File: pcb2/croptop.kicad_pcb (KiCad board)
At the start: 4 copper layers, 190.1 x 107.2 mm, 341 parts, among them J1 TSM-106-01-L-SV, J10 1702474, J11 1702474, J12 1702474, J13 1702474, J14 1702474, J15 TSM-112-01-L-DV, J16 DM3D-SF, J2 0473460001, J3 87583-2010BLF, J4 TSM-102-01-L-DV, J5 686104183422, J6 62684-402100ALF, J7 1702474, J8 1702474, J9 1702474, Q1 BSS138, Q2 BSS84, Q3 Q2319ADS-T1-GE3, Q4 BSS138, Q5 BSS138, Q6 BSS138, SW1 SW_Push, SW2 SW_Push, SW3 SW_Push, SW4 SW_Push, U1 PIC32MX795F512L, U10 TPD4E1U06DBV, U11 TPD4E1U06DBV, U12 TPD4E1U06DBV, U13 TPD4E1U06DBV, U14 TPD4E1U06DBV, U15 TPD4E1U06DBV, U16 TPD4E1U06DBV, U17 TPD4E1U06DBV, U18 74HCT125D653, U19 AP22802AW5, U2 REG71055DDC, U20 AD7799, U21 AP22802AW5, U22 TPD4E1U06DBV, U23 AP22802AW5, U24 TPD4E1U06DBV, U25 TPD4E1U06DBV, U26 TPD4E1U06DBV, U27 DRV8872, U28 DRV8825, U29 AP22802AW5, U3 AP22802AW5, U30 TPD4E1U06DBV, U31 TPD4E1U06DBV, U32 AP22802AW5, U33 AP22802AW5, U34 TPD4E1U06DBV, U35 TPD4E1U06DBV, U36 AP22802AW5, U37 TPD4E1U06DBV, U38 TPD4E1U06DBV, U39 LIS3DSHTR, U4 TPS61169DCK, U40 CAM-M8C-0, U41 Si7006-A20, U5 TPS62131RGT, U6 TPS70950DBV, U7 TPD4E1U06DBV, U8 TPD4E1U06DBV, U9 FT812Q, Y1 ABLS-8.000MHZ-B4-T, Y2 ABLS-12.000MHZ-B2-T, Y3 ABS07-32.768KHZ-1-T

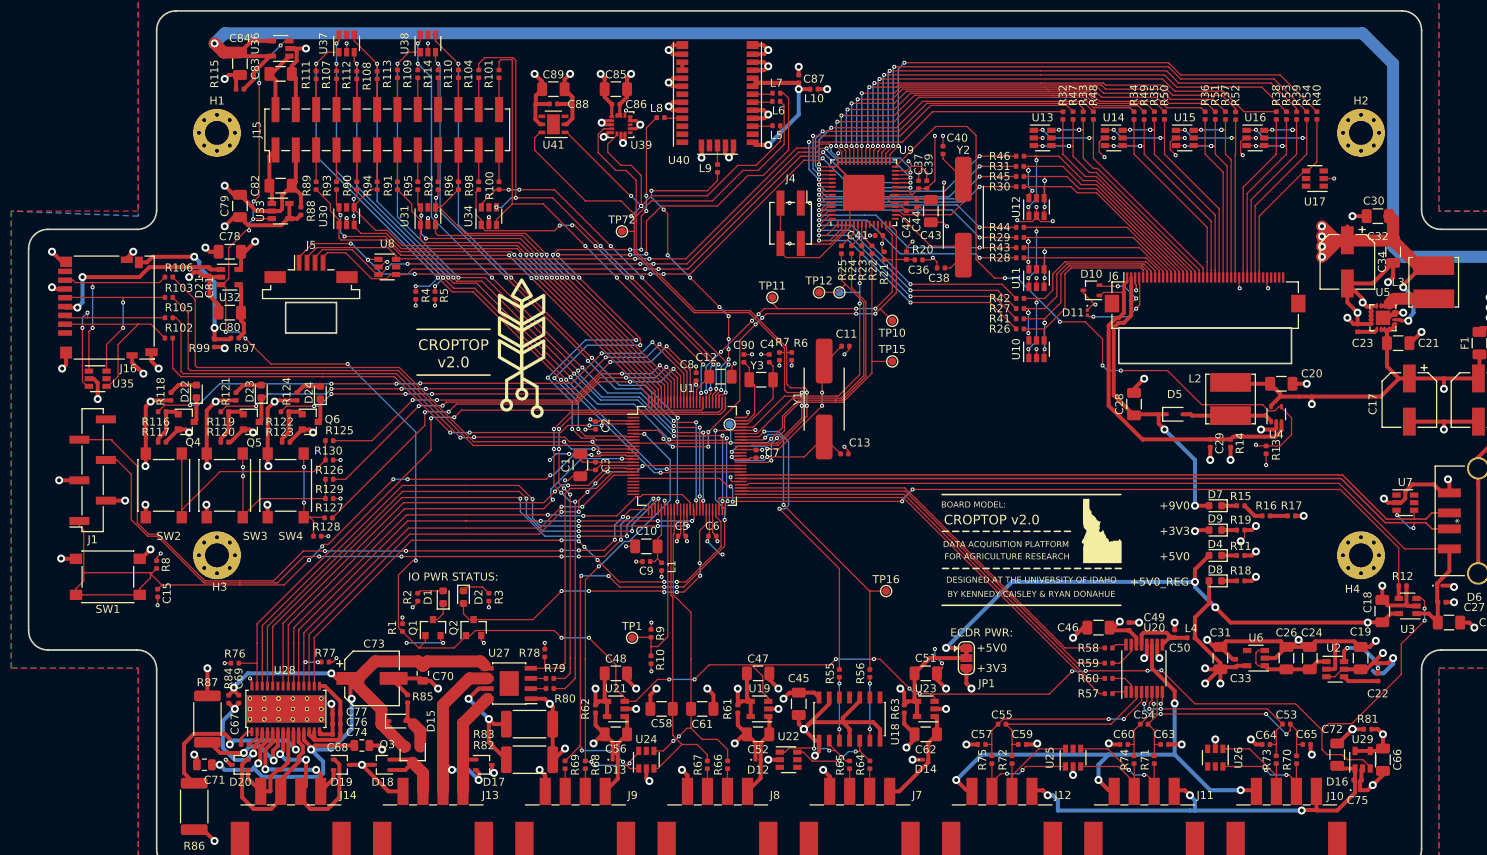
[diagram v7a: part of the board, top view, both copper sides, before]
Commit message: Fixed Screen alignment
- Fixed pin alignment of LCD screen
- Pins now properly align with the ribbon cables of the LCD screen
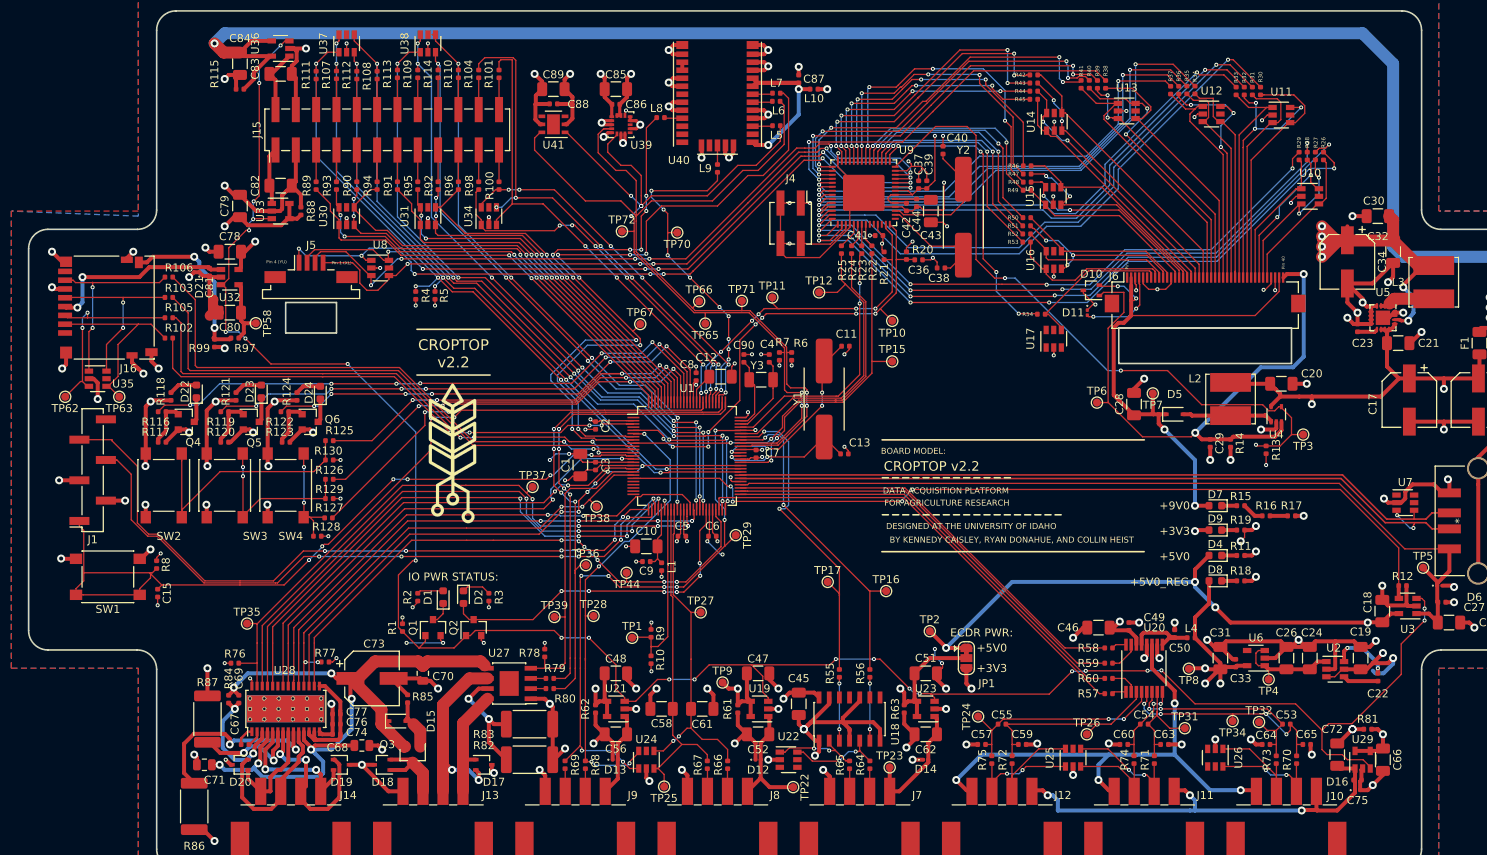
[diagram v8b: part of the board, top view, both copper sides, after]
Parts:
- removed the G*** at (186.4, 120.0)
- removed H1, H2, H3, H4: 3mm, MountingHole:MountingHole_3mm_Pad_Via
- removed TP13, TP14: TestPoint, TestPoint:TestPoint_Pad_D1.0mm
- added TP17: TestPoint, TestPoint:TestPoint_Pad_D1.0mm, F.Cu at (152.2, 126.4)
- added TP2: TestPoint, TestPoint:TestPoint_Pad_D1.0mm, F.Cu at (165.0, 132.5)
- added TP22: TestPoint, TestPoint:TestPoint_Pad_D1.0mm, F.Cu at (147.9, 152.0)
- added TP23: TestPoint, TestPoint:TestPoint_Pad_D1.0mm, F.Cu at (160.0, 149.5)
- added TP24: TestPoint, TestPoint:TestPoint_Pad_D1.0mm, F.Cu at (171.0, 143.2)
- added TP25: TestPoint, TestPoint:TestPoint_Pad_D1.0mm, F.Cu at (131.8, 152.0)
- added TP26: TestPoint, TestPoint:TestPoint_Pad_D1.0mm, F.Cu at (184.6, 145.4)
- added TP27: TestPoint, TestPoint:TestPoint_Pad_D1.0mm, F.Cu at (136.3, 130.2)
- added TP28: TestPoint, TestPoint:TestPoint_Pad_D1.0mm, F.Cu at (122.9, 130.6)
- added TP29: TestPoint, TestPoint:TestPoint_Pad_D1.0mm, F.Cu at (140.7, 120.5)
- added TP3: TestPoint, TestPoint:TestPoint_Pad_D1.0mm, F.Cu at (211.6, 108.0)
- added TP31: TestPoint, TestPoint:TestPoint_Pad_D1.0mm, F.Cu at (196.8, 144.7)
- added TP32: TestPoint, TestPoint:TestPoint_Pad_D1.0mm, F.Cu at (206.1, 143.9)
- added TP34: TestPoint, TestPoint:TestPoint_Pad_D1.0mm, F.Cu at (202.8, 143.8)
- added TP35: TestPoint, TestPoint:TestPoint_Pad_D1.0mm, F.Cu at (79.6, 131.6)
- added TP36: TestPoint, TestPoint:TestPoint_Pad_D1.0mm, F.Cu at (122.0, 124.3)
- added TP37: TestPoint, TestPoint:TestPoint_Pad_D1.0mm, F.Cu at (115.3, 114.5)
- added TP38: TestPoint, TestPoint:TestPoint_Pad_D1.0mm, F.Cu at (123.3, 117.0)
- added TP39: TestPoint, TestPoint:TestPoint_Pad_D1.0mm, F.Cu at (118.0, 130.7)
- added TP4: TestPoint, TestPoint:TestPoint_Pad_D1.0mm, F.Cu at (207.3, 138.6)
- added TP44: TestPoint, TestPoint:TestPoint_Pad_D1.0mm, F.Cu at (127.1, 125.2)
- added TP5: TestPoint, TestPoint:TestPoint_Pad_D1.0mm, F.Cu at (226.6, 124.6)
- added TP58: TestPoint, TestPoint:TestPoint_Pad_D1.0mm, F.Cu at (80.7, 94.0)
- added TP6: TestPoint, TestPoint:TestPoint_Pad_D1.0mm, F.Cu at (185.9, 103.9)
- added TP62: TestPoint, TestPoint:TestPoint_Pad_D1.0mm, F.Cu at (56.9, 103.2)
- added TP63: TestPoint, TestPoint:TestPoint_Pad_D1.0mm, F.Cu at (63.7, 103.2)
- added TP65: TestPoint, TestPoint:TestPoint_Pad_D1.0mm, F.Cu at (136.9, 94.1)
- added TP66: TestPoint, TestPoint:TestPoint_Pad_D1.0mm, F.Cu at (136.1, 91.3)
- added TP67: TestPoint, TestPoint:TestPoint_Pad_D1.0mm, F.Cu at (128.8, 94.1)
- added TP7: TestPoint, TestPoint:TestPoint_Pad_D1.0mm, F.Cu at (192.8, 102.8)
- added TP70: TestPoint, TestPoint:TestPoint_Pad_D1.0mm, F.Cu at (133.4, 82.7)
- added TP71: TestPoint, TestPoint:TestPoint_Pad_D1.0mm, F.Cu at (141.5, 91.2)
- added TP8: TestPoint, TestPoint:TestPoint_Pad_D1.0mm, F.Cu at (197.4, 137.2)
- added TP9: TestPoint, TestPoint:TestPoint_Pad_D1.0mm, F.Cu at (139.1, 138.9)
- moved R26 43.7 mm to (214.2, 73.1), turned to 90 degrees
- moved R27 41.6 mm to (213.2, 73.1), turned to 90 degrees
- moved R54 41.4 mm to (178.9, 92.9), turned to 180 degrees
- moved U10 39.2 mm to (212.5, 78.2), turned to 0 degrees
- moved U17 38.3 mm to (180.5, 96.0), turned to 90 degrees
- moved R28 38.1 mm to (212.2, 73.1), turned to 90 degrees
- moved U11 36.8 mm to (208.9, 68.0), turned to 0 degrees
- moved R29 36.3 mm to (211.1, 73.1), turned to 90 degrees
- moved R53 36.1 mm to (177.1, 83.9), turned to 180 degrees
- moved R30 32.4 mm to (206.3, 65.0), turned to 90 degrees
- moved R31 30.6 mm to (205.3, 65.0), turned to 90 degrees
- moved R41 30.3 mm to (183.9, 64.2), turned to 90 degrees
- moved R52 30.0 mm to (177.1, 82.9), turned to 180 degrees
- moved U16 29.4 mm to (180.5, 86.1), turned to 90 degrees
- moved R40 28.7 mm to (184.9, 64.2)
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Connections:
- J5 pad 1: GPU_X+ -> GPU_Y+
- J5 pad 2: GPU_Y- -> GPU_X+
- J5 pad 3: GPU_X- -> GPU_Y-
- J5 pad 4: GPU_Y+ -> GPU_X-
- J6 pad 1: LCD_K -> Net-(J6-Pad1)
- J6 pad 12: Net-(J6-Pad12) -> DGND
- J6 pad 2: LCD_A -> Net-(J6-Pad2)
- J6 pad 29: DGND -> Net-(J6-Pad29)
- J6 pad 3: DGND -> Net-(J6-Pad3)
- J6 pad 36: DGND -> Net-(J6-Pad36)
- J6 pad 37: Net-(J6-Pad37) -> +3V3
- J6 pad 38: Net-(J6-Pad38) -> DGND
- J6 pad 39: Net-(J6-Pad39) -> LCD_A
- J6 pad 4: +3V3 -> Net-(J6-Pad4)
- J6 pad 40: Net-(J6-Pad40) -> LCD_K
- J6 pad 5: Net-(J6-Pad5) -> DGND
- R26 pad 1: Net-(J6-Pad5) -> Net-(J6-Pad36)
- R27 pad 1: Net-(J6-Pad7) -> Net-(J6-Pad35)
- R28 pad 1: Net-(J6-Pad9) -> Net-(J6-Pad34)
- R29 pad 1: Net-(J6-Pad11) -> Net-(J6-Pad33)
- R30 pad 1: Net-(J6-Pad13) -> Net-(J6-Pad32)
- R31 pad 1: Net-(J6-Pad15) -> Net-(J6-Pad31)
- R32 pad 1: Net-(J6-Pad17) -> Net-(J6-Pad30)
- R33 pad 1: Net-(J6-Pad19) -> Net-(J6-Pad29)
- R34 pad 1: Net-(J6-Pad21) -> Net-(J6-Pad28)
- R35 pad 1: Net-(J6-Pad23) -> Net-(J6-Pad27)
- R36 pad 1: Net-(J6-Pad25) -> Net-(J6-Pad26)
- R37 pad 1: Net-(J6-Pad27) -> Net-(J6-Pad25)
- R38 pad 1: Net-(J6-Pad30) -> Net-(J6-Pad24)
- R39 pad 1: Net-(J6-Pad32) -> Net-(J6-Pad23)
- R40 pad 1: Net-(J6-Pad34) -> Net-(J6-Pad22)
- R41 pad 1: Net-(J6-Pad6) -> Net-(J6-Pad21)
- R42 pad 1: Net-(J6-Pad8) -> Net-(J6-Pad20)
- R43 pad 1: Net-(J6-Pad10) -> Net-(J6-Pad19)
- R44 pad 1: Net-(J6-Pad12) -> Net-(J6-Pad18)
- R45 pad 1: Net-(J6-Pad14) -> Net-(J6-Pad17)
- R47 pad 1: Net-(J6-Pad18) -> Net-(J6-Pad15)
- R48 pad 1: Net-(J6-Pad20) -> Net-(J6-Pad14)
- R49 pad 1: Net-(J6-Pad22) -> Net-(J6-Pad13)
- R50 pad 1: Net-(J6-Pad24) -> Net-(J6-Pad11)
- R51 pad 1: Net-(J6-Pad26) -> Net-(J6-Pad10)
- R52 pad 1: Net-(J6-Pad28) -> Net-(J6-Pad9)
- R53 pad 1: Net-(J6-Pad31) -> Net-(J6-Pad8)
- R54 pad 1: Net-(J6-Pad33) -> Net-(J6-Pad7)
- U10 pad 1: Net-(J6-Pad8) -> Net-(J6-Pad33)
- U10 pad 3: Net-(J6-Pad6) -> Net-(J6-Pad35)
- U10 pad 4: Net-(J6-Pad5) -> Net-(J6-Pad36)
- U10 pad 6: Net-(J6-Pad7) -> Net-(J6-Pad34)
- U11 pad 1: Net-(J6-Pad12) -> Net-(J6-Pad29)
- U11 pad 3: Net-(J6-Pad10) -> Net-(J6-Pad31)
- U11 pad 4: Net-(J6-Pad9) -> Net-(J6-Pad32)
- U11 pad 6: Net-(J6-Pad11) -> Net-(J6-Pad30)
- U12 pad 1: Net-(J6-Pad16) -> Net-(J6-Pad25)
- U12 pad 3: Net-(J6-Pad14) -> Net-(J6-Pad27)
- U12 pad 4: Net-(J6-Pad13) -> Net-(J6-Pad28)
- U12 pad 6: Net-(J6-Pad15) -> Net-(J6-Pad26)
- U13 pad 1: Net-(J6-Pad20) -> Net-(J6-Pad21)
- U13 pad 3: Net-(J6-Pad18) -> Net-(J6-Pad23)
- U13 pad 4: Net-(J6-Pad17) -> Net-(J6-Pad24)
- U13 pad 6: Net-(J6-Pad19) -> Net-(J6-Pad22)
- U14 pad 1: Net-(J6-Pad24) -> Net-(J6-Pad17)
- U14 pad 3: Net-(J6-Pad22) -> Net-(J6-Pad19)
- U14 pad 4: Net-(J6-Pad21) -> Net-(J6-Pad20)
- U14 pad 6: Net-(J6-Pad23) -> Net-(J6-Pad18)
- U15 pad 1: Net-(J6-Pad28) -> Net-(J6-Pad13)
- U15 pad 3: Net-(J6-Pad26) -> Net-(J6-Pad15)
- U15 pad 4: Net-(J6-Pad25) -> Net-(J6-Pad16)
- U15 pad 6: Net-(J6-Pad27) -> Net-(J6-Pad14)
- U16 pad 1: Net-(J6-Pad33) -> Net-(J6-Pad8)
- U16 pad 3: Net-(J6-Pad31) -> Net-(J6-Pad10)
- U16 pad 4: Net-(J6-Pad30) -> Net-(J6-Pad11)
- U16 pad 6: Net-(J6-Pad32) -> Net-(J6-Pad9)
- U17 pad 4: Net-(J6-Pad34) -> Net-(J6-Pad7)
- U8 pad 1: GPU_X+ -> GPU_Y+
- U8 pad 3: GPU_X- -> GPU_Y-
- U8 pad 4: GPU_Y+ -> GPU_X-
- U8 pad 6: GPU_Y- -> GPU_X+
- U9 pad 1: Net-(R41-Pad2) -> Net-(R27-Pad2)
- U9 pad 29: Net-(R40-Pad2) -> Net-(R54-Pad2)
- U9 pad 30: Net-(R54-Pad2) -> Net-(R53-Pad2)
- U9 pad 31: Net-(R39-Pad2) -> Net-(R52-Pad2)
- U9 pad 32: Net-(R53-Pad2) -> Net-(R51-Pad2)
- U9 pad 33: Net-(R38-Pad2) -> Net-(R50-Pad2)
- U9 pad 34: Net-(R52-Pad2) -> Net-(R49-Pad2)
- U9 pad 35: Net-(R37-Pad2) -> Net-(R48-Pad2)
- U9 pad 36: Net-(R51-Pad2) -> Net-(R47-Pad2)
- U9 pad 37: Net-(R36-Pad2) -> Net-(R46-Pad2)
- U9 pad 38: Net-(R50-Pad2) -> Net-(R45-Pad2)
- U9 pad 39: Net-(R35-Pad2) -> Net-(R44-Pad2)
- U9 pad 40: Net-(R49-Pad2) -> Net-(R43-Pad2)
- U9 pad 41: Net-(R34-Pad2) -> Net-(R42-Pad2)
- U9 pad 43: Net-(R48-Pad2) -> Net-(R41-Pad2)
- U9 pad 44: Net-(R33-Pad2) -> Net-(R40-Pad2)
- U9 pad 45: Net-(R47-Pad2) -> Net-(R39-Pad2)
- U9 pad 46: Net-(R32-Pad2) -> Net-(R38-Pad2)
- U9 pad 47: Net-(R46-Pad2) -> Net-(R37-Pad2)
- U9 pad 48: Net-(R31-Pad2) -> Net-(R36-Pad2)
- U9 pad 49: Net-(R45-Pad2) -> Net-(R35-Pad2)
- U9 pad 50: Net-(R30-Pad2) -> Net-(R34-Pad2)
- U9 pad 51: Net-(R44-Pad2) -> Net-(R33-Pad2)
- U9 pad 52: Net-(R29-Pad2) -> Net-(R32-Pad2)
- U9 pad 53: Net-(R43-Pad2) -> Net-(R31-Pad2)
- U9 pad 54: Net-(R28-Pad2) -> Net-(R30-Pad2)
- U9 pad 55: Net-(R42-Pad2) -> Net-(R29-Pad2)
- U9 pad 56: Net-(R27-Pad2) -> Net-(R28-Pad2)
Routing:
- net Net-(R27-Pad2): track 30.9 -> 79.8 mm, vias 2 -> 4
- net Net-(R28-Pad2): track 28.7 -> 76.5 mm, vias 2 -> 4
- net Net-(R26-Pad2): track 33.7 -> 81.1 mm, vias 2 -> 4
- net Net-(R29-Pad2): track 28.1 -> 72.9 mm, vias 2 -> 4
- net Net-(R30-Pad2): track 27.4 -> 71.9 mm
- net Net-(R31-Pad2): track 28.4 -> 70.0 mm
- net Net-(R53-Pad2): track 63.3 -> 27.9 mm
- net LCD_K: track 45.3 -> 75.3 mm, vias 0 -> 2
- net Net-(J6-Pad12): track 29.4 -> 0.00 mm, vias 2 -> 0
- net Net-(R52-Pad2): track 56.9 -> 28.0 mm
- net Net-(R54-Pad2): track 66.1 -> 37.5 mm, vias 2 -> 4
- net Net-(J6-Pad29): track 0.00 -> 28.0 mm
- net Net-(J6-Pad6): track 26.2 -> 0.00 mm, vias 3 -> 0
- net Net-(R51-Pad2): track 54.3 -> 28.8 mm
- net Net-(R32-Pad2): track 40.3 -> 65.6 mm
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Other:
- board text added: "BY KENNEDY CAISLEY, RYAN DONAHUE, AND COLLIN HEIST"
- board text added: "CROPTOP v2.2"
- board text added: "Pin 1"
- board text added: "Pin 1 (XL)"
- board text added: "Pin 4 (YU)"
- board text added: "Pin 40"
- board text removed: "BY KENNEDY CAISLEY & RYAN DONAHUE"
- board text removed: "CROPTOP v2.0"
